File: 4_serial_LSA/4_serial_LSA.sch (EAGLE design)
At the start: 8 parts, among them J1 ED555/2DS

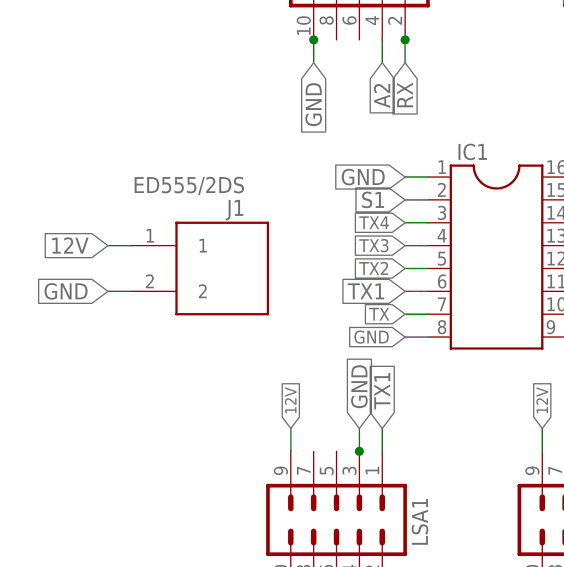
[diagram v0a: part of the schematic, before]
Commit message: add the new molex connetor
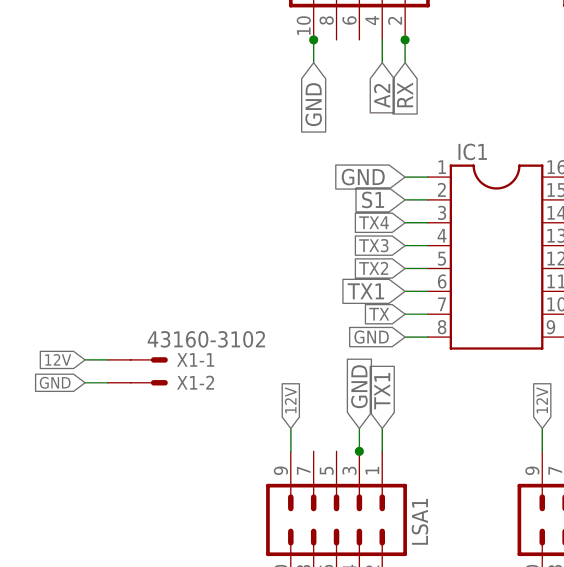
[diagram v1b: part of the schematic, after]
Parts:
- removed J1: ED555/2DS, DC_LOAD_AU:ED555/2DS
- added X1: 43160-3102, con-molex:43160-3102
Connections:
- net 12V: now also X1-1.S@1; no longer J1.1
- net GND: now also X1-2.S@1; no longer J1.2
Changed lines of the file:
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@@
 </part>
 <part name="J6" library="SparkFun-Connectors" deviceset="M06" device="SILK_FEMALE_PTH"/>
-<part name="J1" library="DC_LOAD_AU" library_urn="urn:adsk.eagle:library:220454" deviceset="ED555/2DS" device="" package3d_urn="urn:adsk.eagle:package:220531/3"/>
+<part name="X1" library="con-molex" library_urn="urn:adsk.eagle:library:165" deviceset="43160-*02" device="" technology="31"/>
 </parts>
 <sheets>
@@
 <attribute name="NAME" x="134.62" y="28.702" size="1.778" layer="95"/>
 </instance>
-<instance part="J1" gate="G$1" x="78.74" y="22.86" rot="R180">
-<attribute name="NAME" x="81.28" y="30.48" size="1.778" layer="95" rot="R180"/>
-<attribute name="VALUE" x="81.28" y="33.02" size="1.778" layer="96" rot="R180"/>
+<instance part="X1" gate="-1" x="71.12" y="12.7">
+<attribute name="NAME" x="73.66" y="11.938" size="1.524" layer="95"/>
+<attribute name="VALUE" x="70.358" y="14.097" size="1.778" layer="96"/>
+</instance>
+<instance part="X1" gate="-2" x="71.12" y="10.16">
+<attribute name="NAME" x="73.66" y="9.398" size="1.524" layer="95"/>
 </instance>
 </instances>
@@
 </segment>
 <segment>
-<pinref part="J1" gate="G$1" pin="2"/>
-<wire x1="68.58" y1="20.32" x2="66.04" y2="20.32" width="0.1524" layer="91"/>
-<label x="66.04" y="20.32" size="1.778" layer="95" rot="R180" xref="yes"/>
+<pinref part="X1" gate="-2" pin="S@1"/>
+<wire x1="66.04" y1="10.16" x2="63.5" y2="10.16" width="0.1524" layer="91"/>
+<label x="63.5" y="10.16" size="1.27" layer="95" rot="R180" xref="yes"/>
 </segment>
 </net>
@@
 </segment>
 <segment>
-<pinref part="J1" gate="G$1" pin="1"/>
-<wire x1="68.58" y1="25.4" x2="66.04" y2="25.4" width="0.1524" layer="91"/>
-<label x="66.04" y="25.4" size="1.778" layer="95" rot="R180" xref="yes"/>
-</segment>
-<segment>
 <pinref part="LSA4" gate="G$1" pin="9"/>
 <wire x1="114.3" y1="2.54" x2="114.3" y2="5.08" width="0.1524" layer="91"/>
@@
 <wire x1="88.9" y1="63.5" x2="88.9" y2="66.04" width="0.1524" layer="91"/>
 <label x="88.9" y="66.04" size="1.27" layer="95" rot="R90" xref="yes"/>
+</segment>
+<segment>
+<pinref part="X1" gate="-1" pin="S@1"/>
+<wire x1="66.04" y1="12.7" x2="63.5" y2="12.7" width="0.1524" layer="91"/>
+<label x="63.5" y="12.7" size="1.27" layer="95" rot="R180" xref="yes"/>
 </segment>
 </net>
@@
 with this version.
 </note>
-<note version="8.3" severity="warning">
-Since Version 8.3, EAGLE supports URNs for individual library
-assets (packages, symbols, and devices). The URNs of those assets
-will not be understood (or retained) with this version.
-</note>
-<note version="8.3" severity="warning">
-Since Version 8.3, EAGLE supports the association of 3D packages
-with devices in libraries, schematics, and board files. Those 3D
-packages will not be understood (or retained) with this version.
-</note>
 </compatibility>
